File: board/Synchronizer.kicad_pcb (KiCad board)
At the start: 2 copper layers, 99 x 62 mm, 49 parts, among them J1 POWER, J2 Conn_01x14, J4 Barrel_Jack_Switch, J5 COIL, Q1 2N3904, Q2 2N3906, Q3 IRF9540N, Q4 2N3904, U1 Pico, U2 LM7805_TO220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

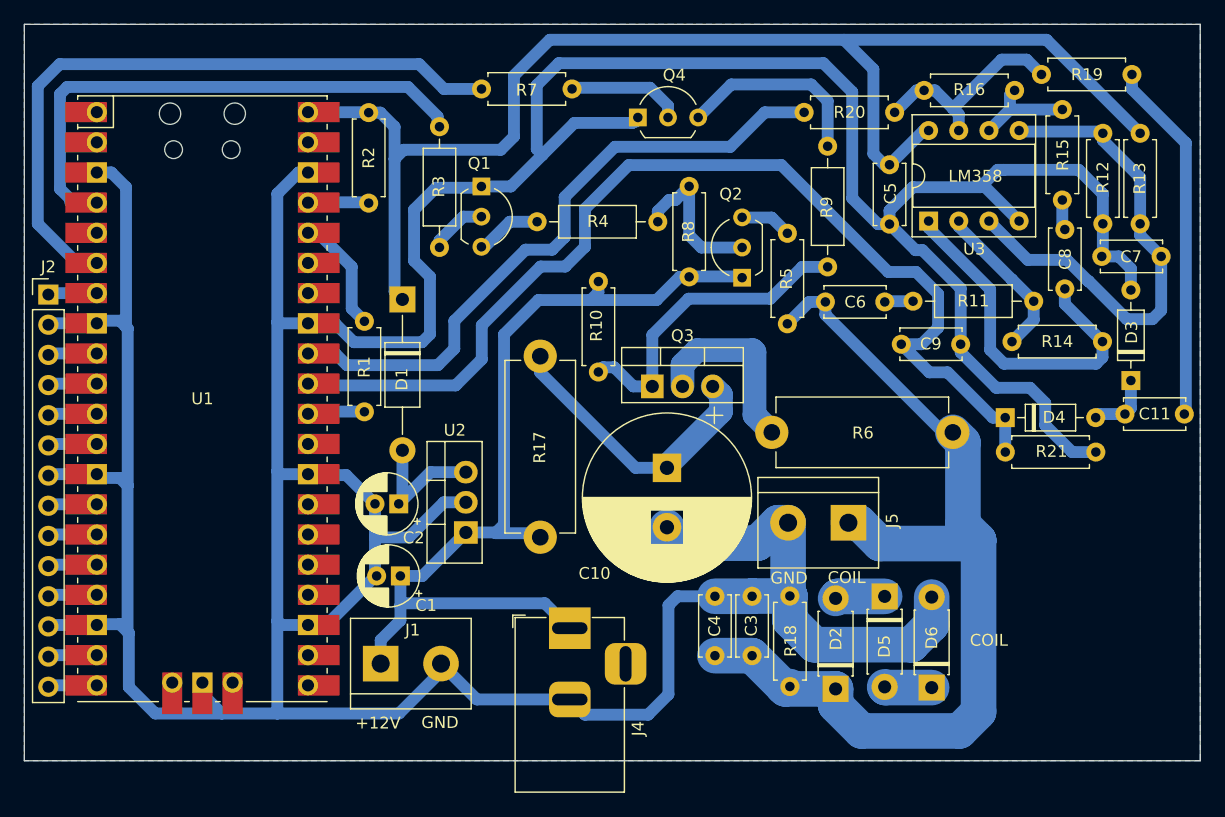
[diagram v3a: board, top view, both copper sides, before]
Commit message: separate coils
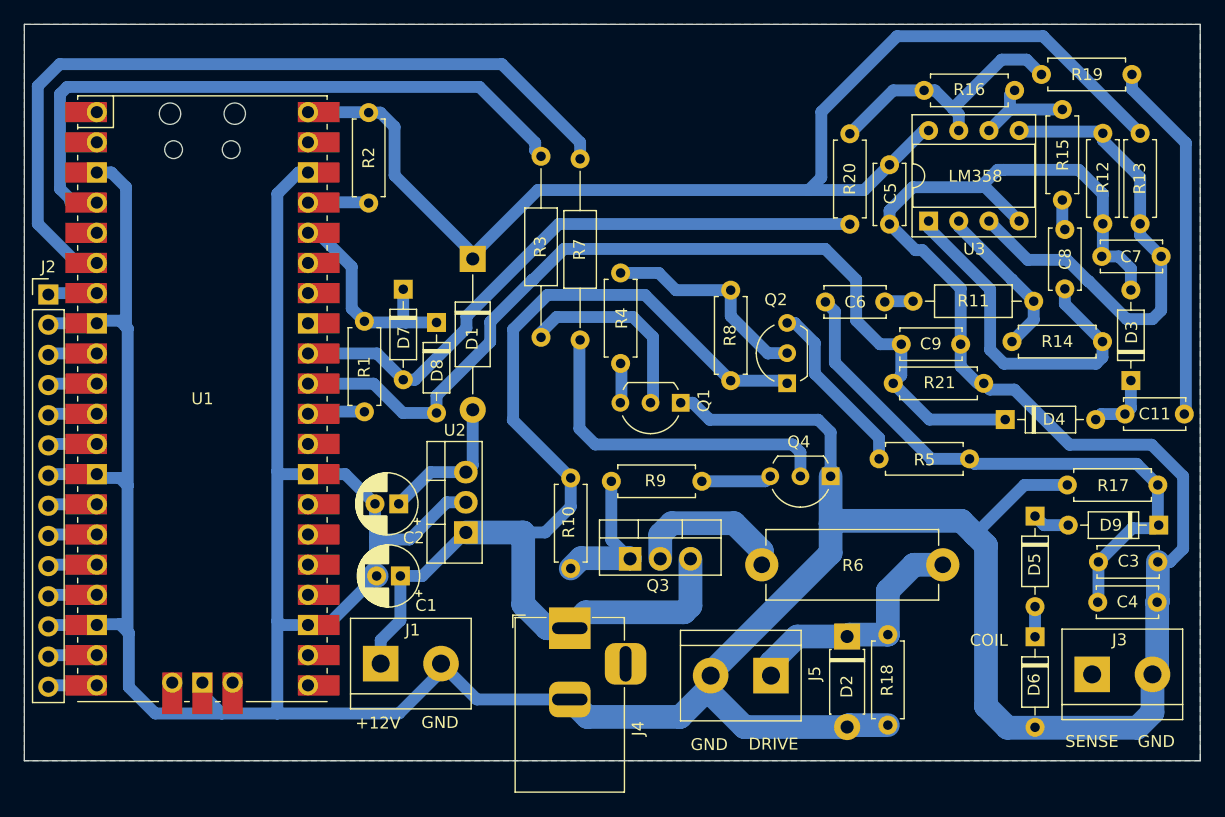
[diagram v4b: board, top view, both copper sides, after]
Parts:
- removed C10: 2200 uF, Capacitor_THT:CP_Radial_D14.0mm_P5.00mm
- added D7: 1N4148, Diode_THT:D_DO-35_SOD27_P7.62mm_Horizontal, F.Cu at (31.9, 22.3)
- added D8: 1N4148, Diode_THT:D_DO-35_SOD27_P7.62mm_Horizontal, F.Cu at (34.7, 25.1)
- added D9: 1N4148, Diode_THT:D_DO-35_SOD27_P7.62mm_Horizontal, F.Cu at (95.5, 42.2)
- added J3: SENSE COIL, TerminalBlock:TerminalBlock_bornier-2_P5.08mm, F.Cu at (89.9, 54.7)
- D5, D6: value UF4007 -> 1N4148; footprint Diode_THT:D_DO-41_SOD81_P7.62mm_Horizontal -> Diode_THT:D_DO-35_SOD27_P7.62mm_Horizontal
- J5: value COIL -> DRIVE COIL
- R17: value 1k -> NC; footprint Resistor_THT:R_Axial_DIN0614_L14.3mm_D5.7mm_P15.24mm_Horizontal -> Resistor_THT:R_Axial_DIN0207_L6.3mm_D2.5mm_P7.62mm_Horizontal
- R3: footprint Resistor_THT:R_Axial_DIN0207_L6.3mm_D2.5mm_P10.16mm_Horizontal -> Resistor_THT:R_Axial_DIN0207_L6.3mm_D2.5mm_P15.24mm_Horizontal
- R4, R9: footprint Resistor_THT:R_Axial_DIN0207_L6.3mm_D2.5mm_P10.16mm_Horizontal -> Resistor_THT:R_Axial_DIN0207_L6.3mm_D2.5mm_P7.62mm_Horizontal
- R7: footprint Resistor_THT:R_Axial_DIN0207_L6.3mm_D2.5mm_P7.62mm_Horizontal -> Resistor_THT:R_Axial_DIN0207_L6.3mm_D2.5mm_P15.24mm_Horizontal
- moved R17 53.1 mm to (95.4, 38.8), turned to 180 degrees
- moved Q4 34.3 mm to (67.9, 38.0), turned to 180 degrees
- moved C4 32.5 mm to (90.4, 48.6), turned to 0 degrees
- moved C3 30.2 mm to (90.4, 45.3), turned to 0 degrees
- moved R9 25.6 mm to (49.4, 38.5), turned to 0 degrees
- moved Q1 24.8 mm to (55.3, 31.9), turned to 180 degrees
- moved R7 21.1 mm to (46.8, 26.6), turned to 90 degrees
- moved R5 20.5 mm to (72.0, 36.6), turned to 0 degrees
- moved R10 16.7 mm to (46.0, 38.2)
- moved Q3 14.6 mm to (51.0, 45.0)
- moved J5 14.4 mm to (62.9, 54.8)
- moved D5 14.4 mm to (85.1, 41.4)
- moved R6 11.2 mm to (77.3, 45.5)
- moved R21 11.1 mm to (73.2, 30.2)
- moved D6 9.69 mm to (85.1, 51.6), turned to -90 degrees
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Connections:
- net Net-(D1-K) renamed OPSUPPLY
- C3 pad 1: Net-(D2-K) -> Net-(D9-K)
- C4 pad 1: Net-(D2-K) -> Net-(D9-K)
- C6 pad 1: Net-(D2-K) -> Net-(D9-K)
- D2 pad 2: Net-(D2-A) -> GND
- D5 pad 1: Net-(D2-A) -> Net-(D5-K)
- Q3 pad 3: Net-(Q3-S) -> +12V
- R17 pad 1: Net-(Q3-S) -> Net-(D9-K)
- R17 pad 2: +12V -> GND
- R5 pad 2: Net-(D2-K) -> Net-(D9-K)
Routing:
- net Net-(D2-K): track 83.0 -> 21.1 mm
- net Net-(D9-K): track 0.00 -> 50.1 mm
- net Net-(Q3-S): track 24.4 -> 0.00 mm
- net Net-(Q4-B): track 9.74 -> 28.9 mm
- net +12V: track 77.7 -> 94.9 mm
- net Net-(Q3-G): track 26.8 -> 12.6 mm
- net Net-(Q1-B): track 4.94 -> 16.7 mm
- net /PULSE: track 56.9 -> 68.5 mm
- net /AMPLITUDE: track 89.6 -> 78.1 mm
- net Net-(Q2-C): track 4.37 -> 15.0 mm
- net Net-(Q4-C): track 16.4 -> 5.93 mm
- net /OSCIL: track 45.7 -> 55.3 mm
- net Net-(D7-K): track 9.90 -> 19.0 mm
- net OPSUPPLY: track 112.6 -> 104.6 mm
- net GND: track 416.8 -> 410.2 mm
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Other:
- board text added: "DRIVE"
- board text added: "SENSE"

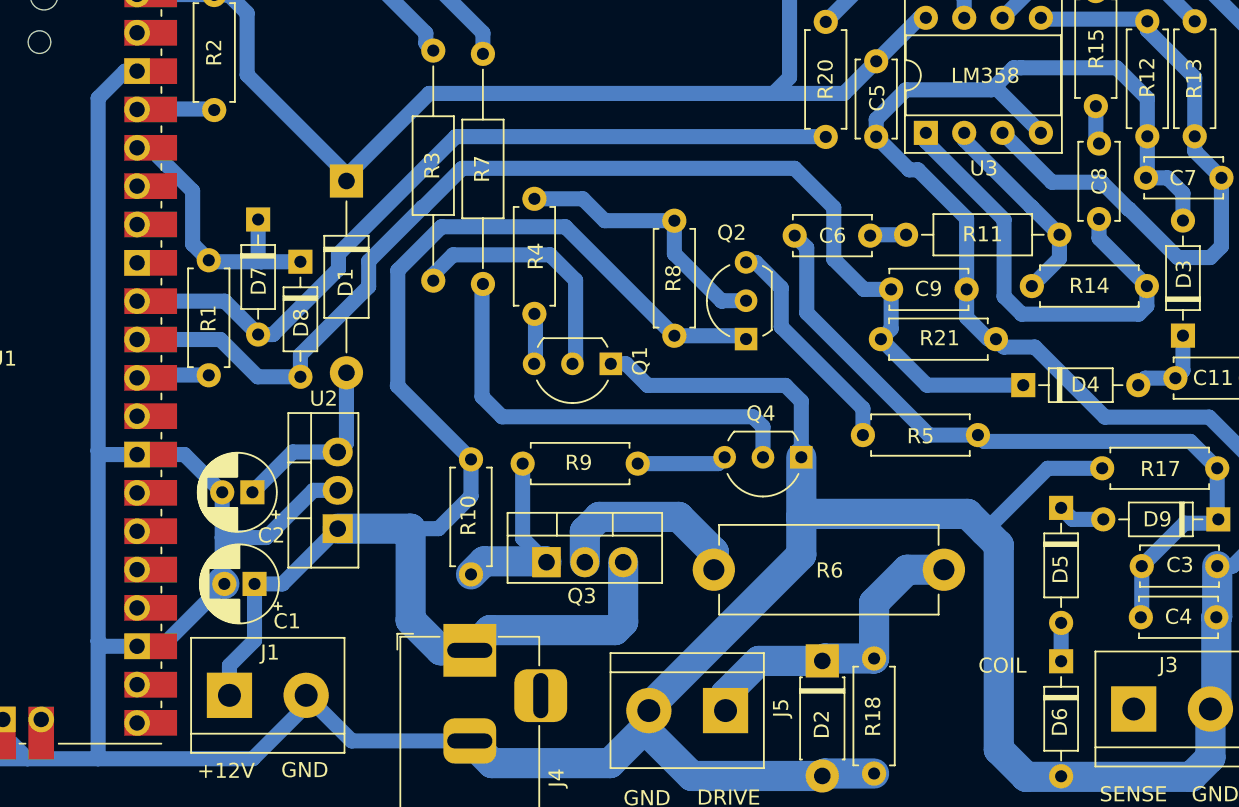
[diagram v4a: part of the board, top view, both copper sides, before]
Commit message: Fixed two unconnected traces
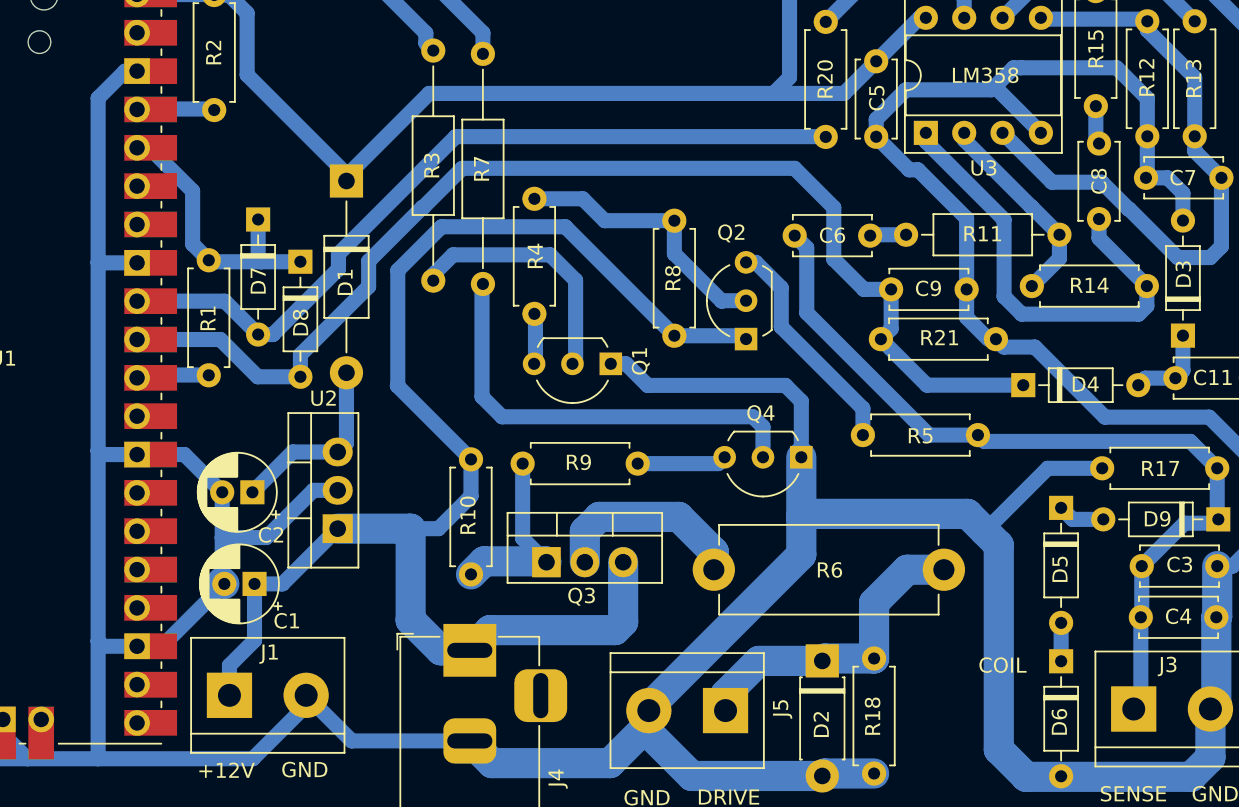
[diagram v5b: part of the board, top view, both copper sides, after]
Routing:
- net Net-(D9-K): track 50.1 -> 56.4 mm
- net GND: track 410.2 -> 412.8 mm
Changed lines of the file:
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@@
   (segment (start 93.16 22.37) (end 93.16 20.56) (width 1) (layer "B.Cu") (net 2))
   (segment (start 57.78 54.61) (end 57.78 54.83) (width 2) (layer "B.Cu") (net 2))
-  (segment (start 21.3 37.62) (end 21.3 14.26) (width 1) (layer "B.Cu") (net 2))
+  (segment (start 21.3 37.62) (end 21.3 25.146) (width 1) (layer "B.Cu") (net 2))
   (segment (start 67.88 44.51) (end 57.78 54.61) (width 2) (layer "B.Cu") (net 2))
   (segment (start 25.53 50.57) (end 29.66 46.44) (width 1) (layer "B.Cu") (net 2))
+  (segment (start 21.3 25.146) (end 21.324 25.17) (width 1) (layer "B.Cu") (net 2))
   (segment (start 6.1 37.87) (end 2.14 37.87) (width 1) (layer "B.Cu") (net 2))
   (segment (start 32.43 43.37) (end 29.52 43.37) (width 1) (layer "B.Cu") (net 2))
@@
   (segment (start 90.8 14.28) (end 88.77 12.25) (width 1) (layer "B.Cu") (net 2))
   (segment (start 80.264 30.226) (end 78.83 28.792) (width 1) (layer "B.Cu") (net 2))
+  (segment (start 21.324 25.17) (end 23.88 25.17) (width 1) (layer "B.Cu") (net 2))
   (segment (start 55.21 58.31) (end 47.39 58.31) (width 2) (layer "B.Cu") (net 2))
   (segment (start 94.9 35.39) (end 97.56 38.05) (width 1) (layer "B.Cu") (net 2))
@@
   (segment (start 27.02 37.87) (end 29.52 40.37) (width 1) (layer "B.Cu") (net 2))
   (segment (start 75.61 19.01) (end 75.03 19.01) (width 1) (layer "B.Cu") (net 2))
+  (segment (start 21.3 25.146) (end 21.3 14.26) (width 1) (layer "B.Cu") (net 2))
   (segment (start 7.32 12.47) (end 6.1 12.47) (width 1) (layer "B.Cu") (net 2))
   (segment (start 80.48 13.71) (end 74.8 13.71) (width 1) (layer "B.Cu") (net 2))
@@
   (segment (start 45.42 18.91) (end 67.43 18.91) (width 1) (layer "B.Cu") (net 9))
   (segment (start 90.43 45.26) (end 93.272 42.418) (width 1) (layer "B.Cu") (net 10))
+  (segment (start 90.37 54.255) (end 89.9 54.725) (width 1) (layer "B.Cu") (net 10))
   (segment (start 68.24 24.17) (end 67.44 23.37) (width 1) (layer "B.Cu") (net 10))
   (segment (start 76.34 36.58) (end 68.24 28.48) (width 1) (layer "B.Cu") (net 10))
@@
   (segment (start 95.25 42.418) (end 95.504 42.164) (width 1) (layer "B.Cu") (net 10))
   (segment (start 95.43 42.09) (end 95.504 42.164) (width 1) (layer "B.Cu") (net 10))
+  (segment (start 90.37 48.65) (end 90.37 54.255) (width 1) (layer "B.Cu") (net 10))
   (segment (start 79.58 36.58) (end 76.34 36.58) (width 1) (layer "B.Cu") (net 10))
   (segment (start 93.65 37) (end 95.43 38.78) (width 1) (layer "B.Cu") (net 10))
